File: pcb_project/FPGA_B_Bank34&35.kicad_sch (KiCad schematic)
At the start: 14 parts, among them U1 XC7A100T-FTG256, Y2 XLH736025.175000I

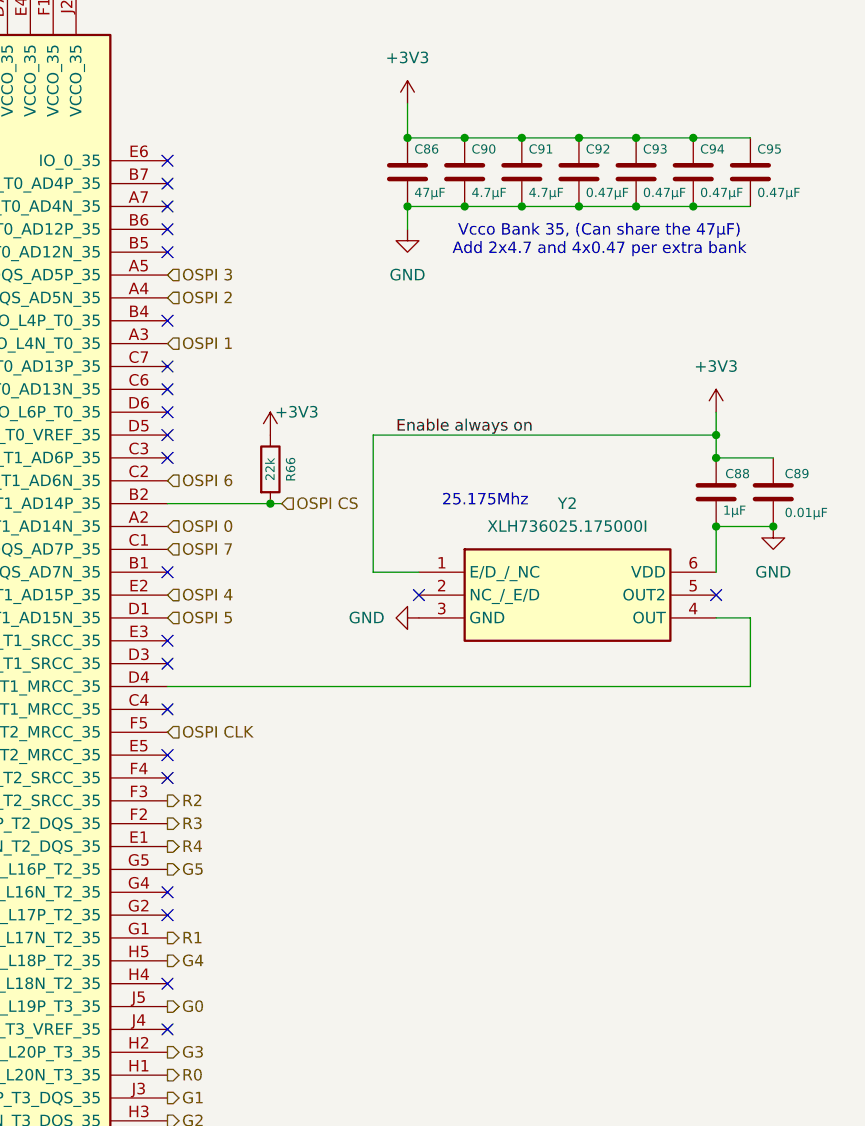
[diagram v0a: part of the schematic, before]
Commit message: Add GPIO pins for MCU and FPGA
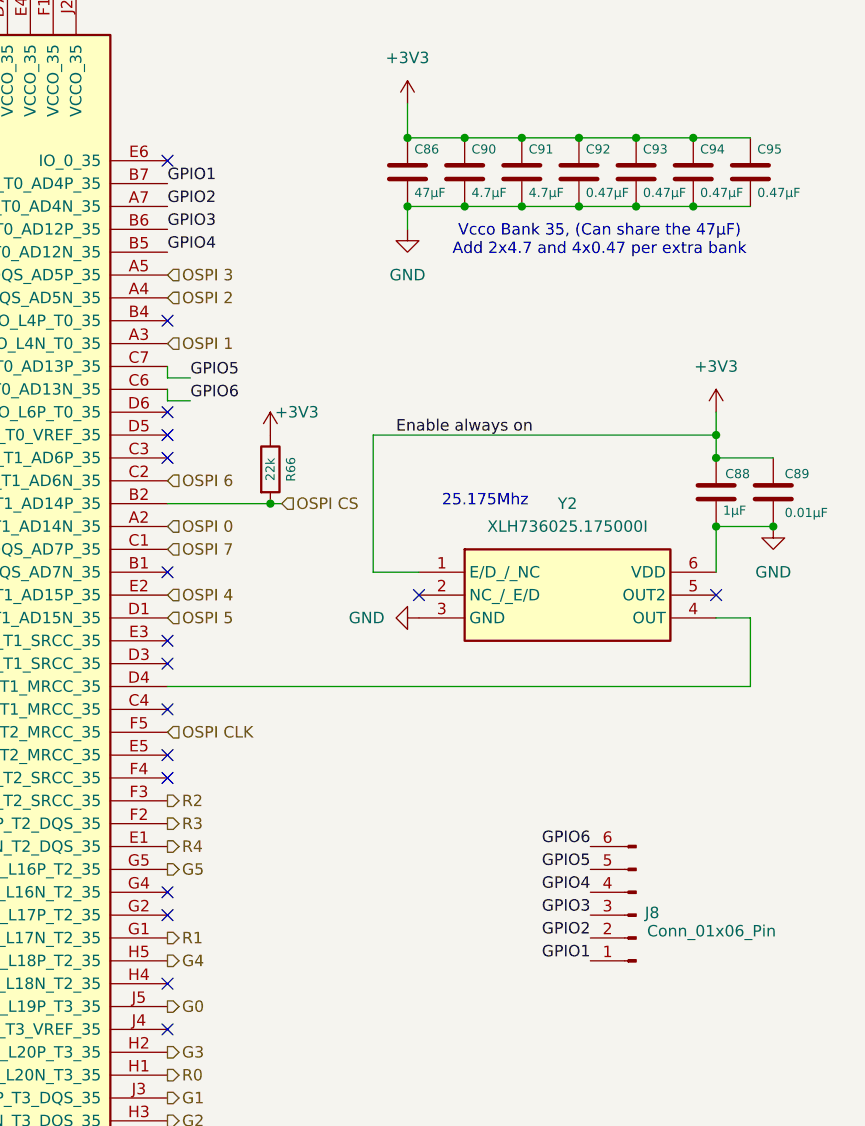
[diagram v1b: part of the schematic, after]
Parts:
- added J8: Conn_01x06_Pin, Connector_PinHeader_2.54mm:PinHeader_1x06_P2.54mm_Vertical, symbol Connector:Conn_01x06_Pin
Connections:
- net GPIO2: now reaches U1.A7 (IO_L1N_T0_AD4N_35)
- net GPIO2: now also J8.2 (Pin_2)
- net GPIO4: now reaches U1.B5 (IO_L2N_T0_AD12N_35)
- net GPIO4: now also J8.4 (Pin_4)
- net GPIO3: now reaches U1.B6 (IO_L2P_T0_AD12P_35)
- net GPIO3: now also J8.3 (Pin_3)
- net GPIO1: now reaches U1.B7 (IO_L1P_T0_AD4P_35)
- net GPIO1: now also J8.1 (Pin_1)
- net GPIO6: now reaches U1.C6 (IO_L5N_T0_AD13N_35)
- net GPIO6: now also J8.6 (Pin_6)
- net GPIO5: now reaches U1.C7 (IO_L5P_T0_AD13P_35)
- net GPIO5: now also J8.5 (Pin_5)
- no-connect marks 43 -> 37
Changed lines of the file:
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@@
-	)
-	(no_connect
-		(at 196.85 59.69)
 	)
 	(no_connect
@@
 	)
 	(no_connect
-		(at 196.85 36.83)
-	)
-	(no_connect
 		(at 196.85 125.73)
 	)
@@
 	)
 	(no_connect
-		(at 196.85 39.37)
-	)
-	(no_connect
 		(at 95.25 57.15)
 	)
@@
 	)
 	(no_connect
-		(at 196.85 57.15)
-	)
-	(no_connect
 		(at 196.85 87.63)
 	)
@@
 	)
 	(no_connect
-		(at 196.85 44.45)
-	)
-	(no_connect
 		(at 196.85 52.07)
 	)
@@
 	)
 	(no_connect
-		(at 196.85 41.91)
-	)
-	(no_connect
 		(at 95.25 80.01)
 	)
@@
 	(wire
 		(pts
+			(xy 196.85 58.42) (xy 196.85 57.15)
+		)
+		(stroke
+			(width 0)
+			(type default)
+		)
+	)
+	(wire
+		(pts
 			(xy 248.92 39.37) (xy 255.27 39.37)
 		)
@@
 	(wire
 		(pts
+			(xy 199.39 58.42) (xy 196.85 58.42)
+		)
+		(stroke
+			(width 0)
+			(type default)
+		)
+	)
+	(wire
+		(pts
 			(xy 181.61 13.97) (xy 184.15 13.97)
 		)
@@
 	(wire
 		(pts
+			(xy 196.85 60.96) (xy 196.85 59.69)
+		)
+		(stroke
+			(width 0)
+			(type default)
+		)
+	)
+	(wire
+		(pts
 			(xy 236.22 39.37) (xy 242.57 39.37)
 		)
@@
 	(wire
 		(pts
+			(xy 199.39 60.96) (xy 196.85 60.96)
+		)
+		(stroke
+			(width 0)
+			(type default)
+		)
+	)
+	(wire
+		(pts
 			(xy 224.79 80.01) (xy 219.71 80.01)
 		)
@@
 			(width 0)
 			(type default)
+		)
+	)
+	(label "GPIO4"
+		(at 196.85 44.45 0)
+		(effects
+			(font
+				(size 1.27 1.27)
+			)
+			(justify left bottom)
+		)
+	)
+	(label "GPIO1"
+		(at 243.84 123.19 180)
+		(effects
+			(font
+				(size 1.27 1.27)
+			)
+			(justify right bottom)
+		)
+	)
+	(label "GPIO3"
+		(at 196.85 41.91 0)
+		(effects
+			(font
+				(size 1.27 1.27)
+			)
+			(justify left bottom)
+		)
+	)
+	(label "GPIO2"
+		(at 196.85 39.37 0)
+		(effects
+			(font
+				(size 1.27 1.27)
+			)
+			(justify left bottom)
+		)
+	)
+	(label "GPIO5"
+		(at 243.84 113.03 180)
+		(effects
+			(font
+				(size 1.27 1.27)
+			)
+			(justify right bottom)
+		)
+	)
+	(label "GPIO4"
+		(at 243.84 115.57 180)
+		(effects
+			(font
+				(size 1.27 1.27)
+			)
+			(justify right bottom)
+		)
+	)
+	(label "GPIO5"
+		(at 199.39 58.42 0)
+		(effects
+			(font
+				(size 1.27 1.27)
+			)
+			(justify left bottom)
+		)
+	)
+	(label "GPIO2"
+		(at 243.84 120.65 180)
+		(effects
+			(font
+				(size 1.27 1.27)
+			)
+			(justify right bottom)
+		)
+	)
+	(label "GPIO6"
+		(at 243.84 110.49 180)
+		(effects
+			(font
+				(size 1.27 1.27)
+			)
+			(justify right bottom)
+		)
+	)
+	(label "GPIO6"
+		(at 199.39 60.96 0)
+		(effects
+			(font
+				(size 1.27 1.27)
+			)
+			(justify left bottom)
 		)
 	)
 	(label "Enable always on"
 		(at 222.25 64.77 0)
+		(effects
+			(font
+				(size 1.27 1.27)
+			)
+			(justify left bottom)
+		)
+	)
+	(label "GPIO3"
+		(at 243.84 118.11 180)
+		(effects
+			(font
+				(size 1.27 1.27)
+			)
+			(justify right bottom)
+		)
+	)
+	(label "GPIO1"
+		(at 196.85 36.83 0)
 		(effects
 			(font
@@
 					(unit 1)
 				)
+			)
+		)
+	)
+	(symbol
+		(lib_id "Connector:Conn_01x06_Pin")
+		(at 248.92 118.11 180)
+		(unit 1)
+		(exclude_from_sim no)
+		(in_bom yes)
+		(on_board yes)
+		(dnp no)
+		(property "Reference" "J8"
+			(at 250.698 117.856 0)
+			(effects
+				(font
+					(size 1.27 1.27)
+				)
+			)
+		)
+		(property "Value" "Conn_01x06_Pin"
+			(at 257.302 119.888 0)
+			(effects
+				(font
+					(size 1.27 1.27)
+				)
+			)
+		)
+		(property "Footprint" "Connector_PinHeader_2.54mm:PinHeader_1x06_P2.54mm_Vertical"
+			(at 248.92 118.11 0)
+			(effects
+				(font
+					(size 1.27 1.27)
+				)
+				(hide yes)
+			)
+		)
+		(property "Datasheet" "~"
+			(at 248.92 118.11 0)
+			(effects
+				(font
+					(size 1.27 1.27)
+				)
+				(hide yes)
+			)
+		)
+		(property "Description" "Generic connector, single row, 01x06, script generated"
+			(at 248.92 118.11 0)
+			(effects
+				(font
+					(size 1.27 1.27)
+				)
+				(hide yes)
+			)
+		)
+		(pin "2"
+		)
+		(pin "6"
+		)
+		(pin "1"
+		)
+		(pin "3"
+		)
+		(pin "5"
+		)
+		(pin "4"
+		)
+		(instances
+			(project ""
+				(path "/98f80f66-4595-4d0f-90ca-59b2db6f447b/8bdc4eb6-105b-4ccb-b86f-5b5221dfef47/1311c77a-2e60-4e70-8492-84cf53095df7"
+					(reference "J8")
+					(unit 1)
+				)

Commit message: Changed capacitor sizes. Now it's even more difficult
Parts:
- C90, C91: footprint Capacitor_SMD:C_0402_1005Metric_Pad0.74x0.62mm_HandSolder -> Capacitor_SMD:C_0603_1608Metric_Pad1.08x0.95mm_HandSolder
- C93, C94, C95: footprint Capacitor_SMD:C_01005_0402Metric_Pad0.57x0.30mm_HandSolder -> Capacitor_SMD:C_0603_1608Metric_Pad1.08x0.95mm_HandSolder
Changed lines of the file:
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@@
 			)
 		)
-		(property "Footprint" "Capacitor_SMD:C_01005_0402Metric_Pad0.57x0.30mm_HandSolder"
+		(property "Footprint" "Capacitor_SMD:C_0603_1608Metric_Pad1.08x0.95mm_HandSolder"
 			(at 262.5852 39.37 0)
 			(effects
@@
 			)
 		)
-		(property "Footprint" "Capacitor_SMD:C_01005_0402Metric_Pad0.57x0.30mm_HandSolder"
+		(property "Footprint" "Capacitor_SMD:C_0603_1608Metric_Pad1.08x0.95mm_HandSolder"
 			(at 256.2352 39.37 0)
 			(effects
@@
 			)
 		)
-		(property "Footprint" "Capacitor_SMD:C_01005_0402Metric_Pad0.57x0.30mm_HandSolder"
+		(property "Footprint" "Capacitor_SMD:C_0603_1608Metric_Pad1.08x0.95mm_HandSolder"
 			(at 249.8852 39.37 0)
 			(effects
@@
 			)
 		)
-		(property "Footprint" "Capacitor_SMD:C_0402_1005Metric_Pad0.74x0.62mm_HandSolder"
+		(property "Footprint" "Capacitor_SMD:C_0603_1608Metric_Pad1.08x0.95mm_HandSolder"
 			(at 237.1852 39.37 0)
 			(effects
@@
 			)
 		)
-		(property "Footprint" "Capacitor_SMD:C_0402_1005Metric_Pad0.74x0.62mm_HandSolder"
+		(property "Footprint" "Capacitor_SMD:C_0603_1608Metric_Pad1.08x0.95mm_HandSolder"
 			(at 230.8352 39.37 0)
 			(effects

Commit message: Fix remaining FPGA capasitors
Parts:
- C92: footprint Capacitor_SMD:C_01005_0402Metric_Pad0.57x0.30mm_HandSolder -> Capacitor_SMD:C_0603_1608Metric_Pad1.08x0.95mm_HandSolder
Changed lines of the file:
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@@
 			)
 		)
-		(property "Footprint" "Capacitor_SMD:C_01005_0402Metric_Pad0.57x0.30mm_HandSolder"
+		(property "Footprint" "Capacitor_SMD:C_0603_1608Metric_Pad1.08x0.95mm_HandSolder"
 			(at 243.5352 39.37 0)
 			(effects

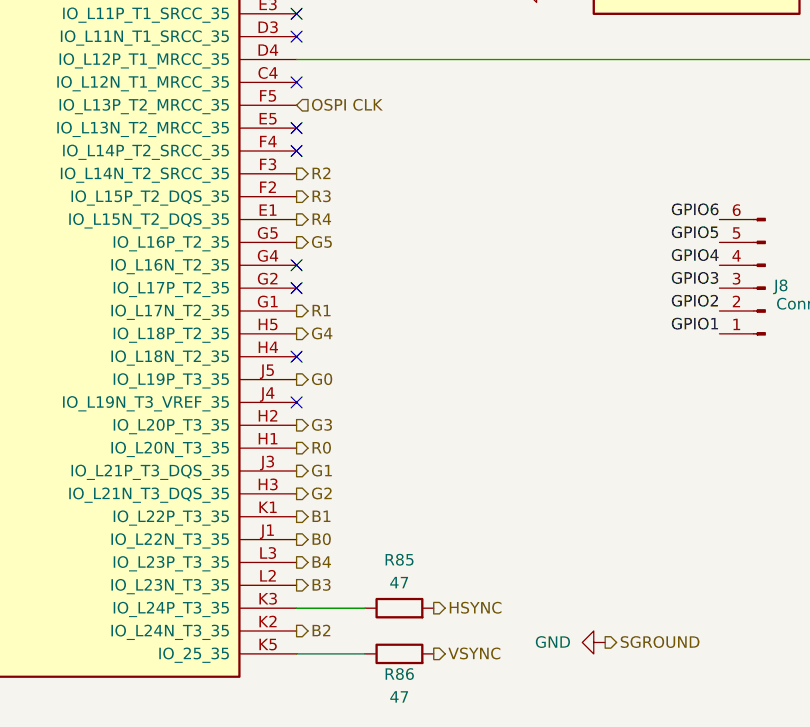
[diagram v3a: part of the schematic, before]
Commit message: Reconnect VGA and FPGA
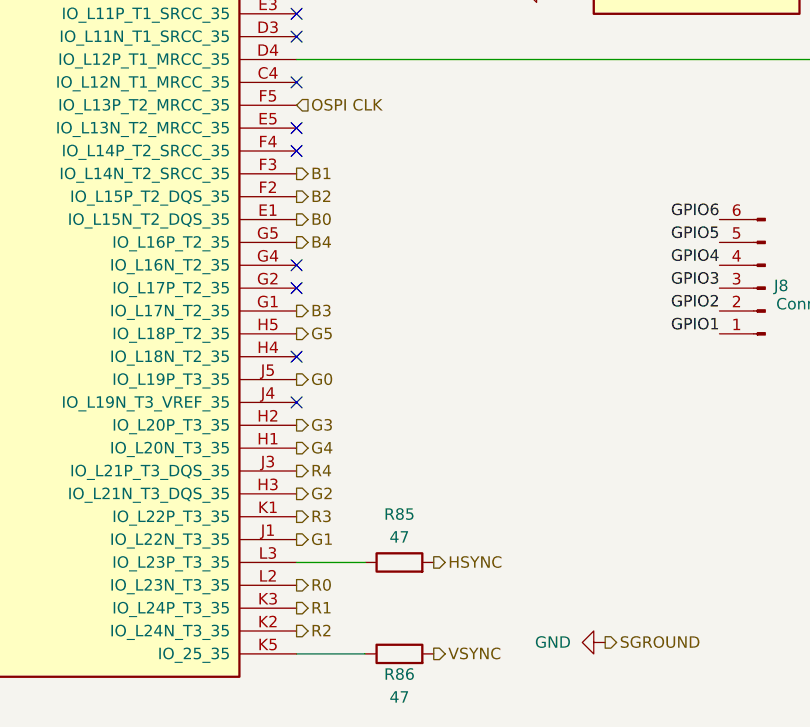
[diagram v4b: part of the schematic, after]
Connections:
- net B0: now also U1.E1 (IO_L15N_T2_DQS_35); no longer U1.J1 (IO_L22N_T3_35)
- net B1: now also U1.F3 (IO_L14N_T2_SRCC_35); no longer U1.K1 (IO_L22P_T3_35)
- net B2: now also U1.F2 (IO_L15P_T2_DQS_35); no longer U1.K2 (IO_L24N_T3_35)
- net B3: now also U1.G1 (IO_L17N_T2_35); no longer U1.L2 (IO_L23N_T3_35)
- net B4: now also U1.G5 (IO_L16P_T2_35); no longer U1.L3 (IO_L23P_T3_35)
- net G1: now also U1.J1 (IO_L22N_T3_35); no longer U1.J3 (IO_L21P_T3_DQS_35)
- net G4: now also U1.H1 (IO_L20N_T3_35); no longer U1.H5 (IO_L18P_T2_35)
- net G5: now also U1.H5 (IO_L18P_T2_35); no longer U1.G5 (IO_L16P_T2_35)
- net R0: now also U1.L2 (IO_L23N_T3_35); no longer U1.H1 (IO_L20N_T3_35)
- net R1: now also U1.K3 (IO_L24P_T3_35); no longer U1.G1 (IO_L17N_T2_35)
- net R2: now also U1.K2 (IO_L24N_T3_35); no longer U1.F3 (IO_L14N_T2_SRCC_35)
- net R3: now also U1.K1 (IO_L22P_T3_35); no longer U1.F2 (IO_L15P_T2_DQS_35)
- net R4: now also U1.J3 (IO_L21P_T3_DQS_35); no longer U1.E1 (IO_L15N_T2_DQS_35)
- net at R85.1: now also U1.L3 (IO_L23P_T3_35); no longer U1.K3 (IO_L24P_T3_35)
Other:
- moved on the sheet: R85
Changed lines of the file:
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@@
 	(wire
 		(pts
-			(xy 196.85 153.67) (xy 204.47 153.67)
+			(xy 196.85 148.59) (xy 204.47 148.59)
 		)
 		(stroke
@@
 	(hierarchical_label "R4"
 		(shape output)
-		(at 196.85 110.49 0)
+		(at 196.85 138.43 0)
 		(effects
 			(font
@@
 	(hierarchical_label "B2"
 		(shape output)
-		(at 196.85 156.21 0)
+		(at 196.85 107.95 0)
 		(effects
 			(font
@@
 	(hierarchical_label "R3"
 		(shape output)
-		(at 196.85 107.95 0)
+		(at 196.85 143.51 0)
 		(effects
 			(font
@@
 	(hierarchical_label "G4"
 		(shape output)
-		(at 196.85 123.19 0)
+		(at 196.85 135.89 0)
 		(effects
 			(font
@@
 	(hierarchical_label "B3"
 		(shape output)
-		(at 196.85 151.13 0)
+		(at 196.85 120.65 0)
 		(effects
 			(font
@@
 	(hierarchical_label "B4"
 		(shape output)
-		(at 196.85 148.59 0)
+		(at 196.85 113.03 0)
 		(effects
 			(font
@@
 	(hierarchical_label "B1"
 		(shape output)
-		(at 196.85 143.51 0)
+		(at 196.85 105.41 0)
 		(effects
 			(font
@@
 	(hierarchical_label "G1"
 		(shape output)
-		(at 196.85 138.43 0)
+		(at 196.85 146.05 0)
 		(effects
 			(font
@@
 	(hierarchical_label "R2"
 		(shape output)
-		(at 196.85 105.41 0)
+		(at 196.85 156.21 0)
 		(effects
 			(font
@@
 	(hierarchical_label "G5"
 		(shape output)
-		(at 196.85 113.03 0)
+		(at 196.85 123.19 0)
 		(effects
 			(font
@@
 	(hierarchical_label "R0"
 		(shape output)
-		(at 196.85 135.89 0)
+		(at 196.85 151.13 0)
 		(effects
 			(font
@@
 	(hierarchical_label "HSYNC"
 		(shape output)
-		(at 212.09 153.67 0)
+		(at 212.09 148.59 0)
 		(effects
 			(font
@@
 	(hierarchical_label "B0"
 		(shape output)
-		(at 196.85 146.05 0)
+		(at 196.85 110.49 0)
 		(effects
 			(font
@@
 	(hierarchical_label "R1"
 		(shape output)
-		(at 196.85 120.65 0)
+		(at 196.85 153.67 0)
 		(effects
 			(font
@@
 	(symbol
 		(lib_id "Device:R")
-		(at 208.28 153.67 90)
+		(at 208.28 148.59 90)
 		(unit 1)
 		(exclude_from_sim no)
@@
 		(dnp no)
 		(property "Reference" "R85"
-			(at 208.28 148.336 90)
+			(at 208.28 143.256 90)
 			(effects
 				(font
@@
 		)
 		(property "Value" "47"
-			(at 208.28 150.876 90)
+			(at 208.28 145.796 90)
 			(effects
 				(font
@@
 		)
 		(property "Footprint" "Resistor_SMD:R_0805_2012Metric_Pad1.20x1.40mm_HandSolder"
-			(at 208.28 155.448 90)
+			(at 208.28 150.368 90)
 			(effects
 				(font
@@
 		)
 		(property "Datasheet" "~"
-			(at 208.28 153.67 0)
+			(at 208.28 148.59 0)
 			(effects
 				(font
@@
 		)
 		(property "Description" "Resistor"
-			(at 208.28 153.67 0)
-			(effects
-				(font
+			(at 208.28 148.59 0)
+			(effects
+				(font

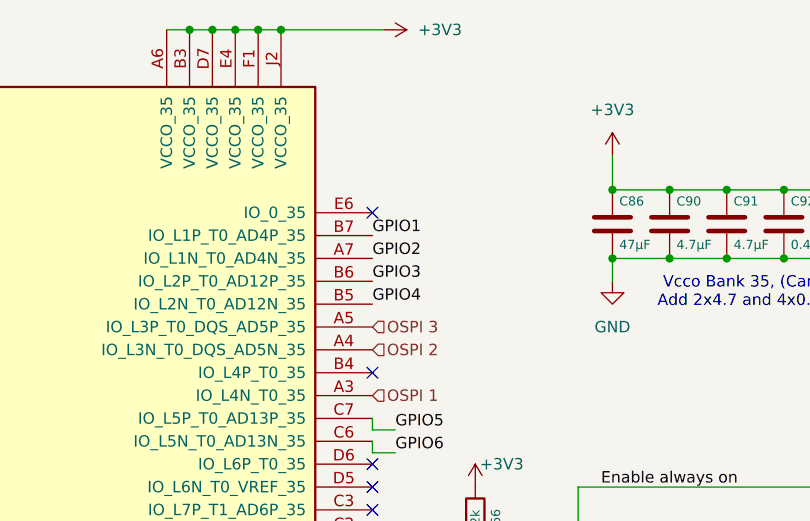
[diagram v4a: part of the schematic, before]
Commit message: Reconnect FPGA GPIO
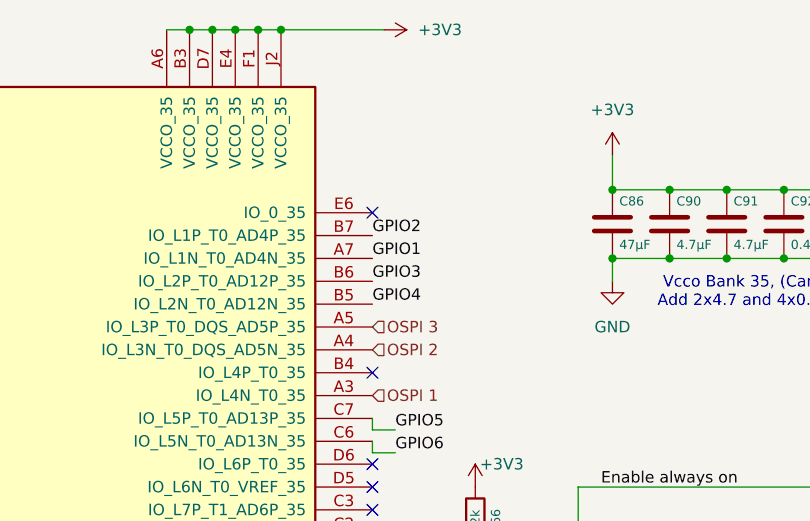
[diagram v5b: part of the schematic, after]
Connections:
- net GPIO1: now also U1.A7 (IO_L1N_T0_AD4N_35); no longer U1.B7 (IO_L1P_T0_AD4P_35)
- net GPIO2: now also U1.B7 (IO_L1P_T0_AD4P_35); no longer U1.A7 (IO_L1N_T0_AD4N_35)
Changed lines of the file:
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@@
 	)
 	(label "GPIO2"
-		(at 196.85 39.37 0)
+		(at 196.85 36.83 0)
 		(effects
 			(font
@@
 	)
 	(label "GPIO1"
-		(at 196.85 36.83 0)
+		(at 196.85 39.37 0)
 		(effects
 			(font
